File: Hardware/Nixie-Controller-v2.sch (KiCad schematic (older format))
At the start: 219 parts, among them J7 12V DC JACK, J8 RST, U1 MAX1771, U10 74HC4067, U11 M41T01, U12 STM32F103C8, U13 OPA180, U14 74HC4067, U15 OPA180, U16 74HC4067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

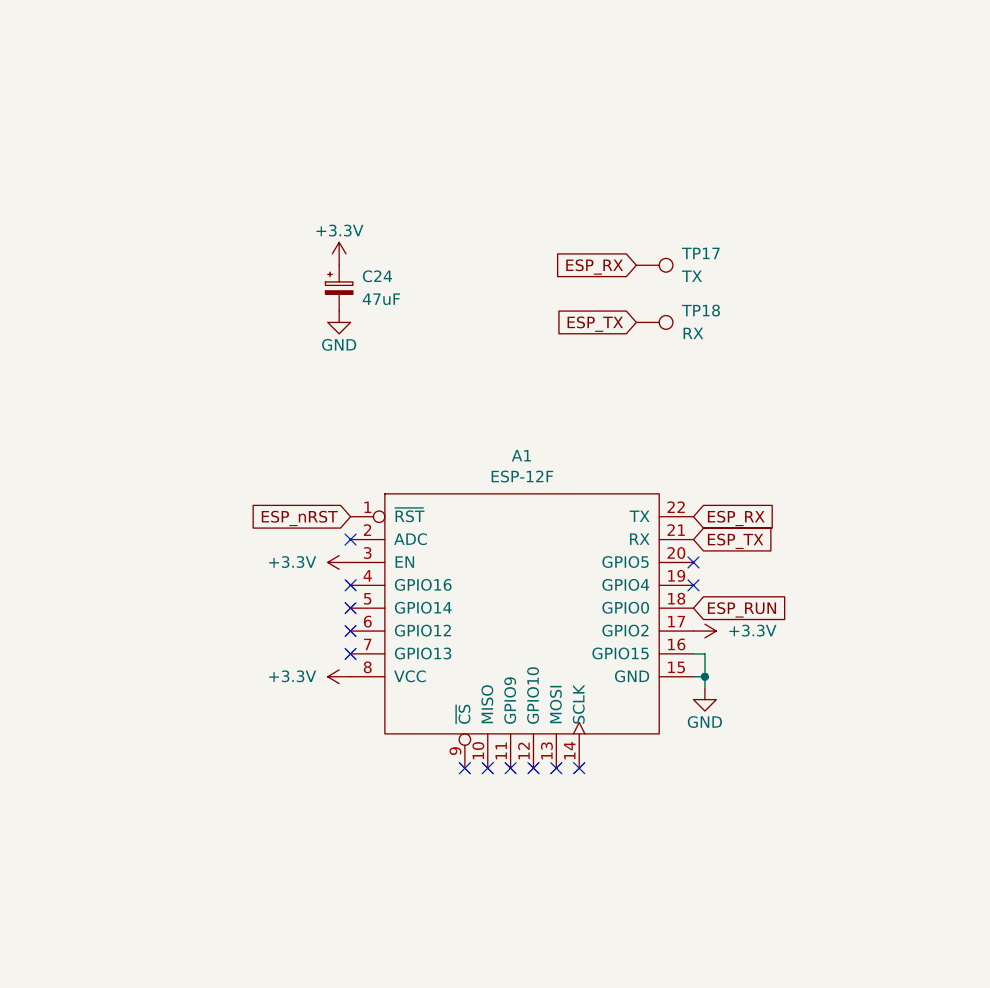
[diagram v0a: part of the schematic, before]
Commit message: Switch to ESP32-WROOM-32E wifi module
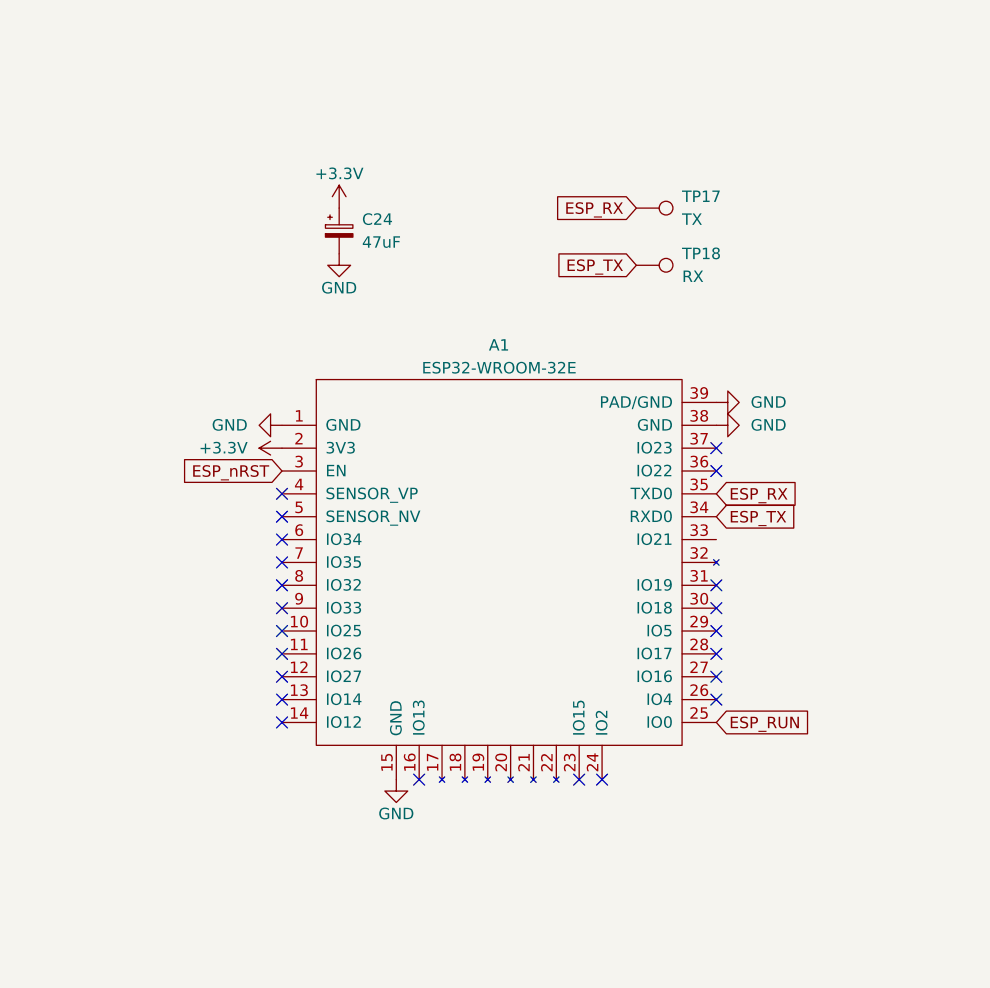
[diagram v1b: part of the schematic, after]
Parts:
- removed A1: ESP-12F, RF_Module:ESP-12E, symbol Nixie-Controller-v2:ESP-12F
- added A1: ESP32-WROOM-32E, RF_Module:ESP32-WROOM-32, symbol Nixie-Controller-v2:ESP32-WROOM-32E
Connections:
- net +3V3: now also A1.2 (3V3)
- net ESP_RUN: now also A1.25 (IO0)
- net ESP_RX: now also A1.35 (TXD0)
- net ESP_TX: now also A1.34 (RXD0)
- net ESP_nRST: now also A1.3 (EN)
- net GND: now also A1.1 (GND), A1.15 (GND), A1.38 (GND), A1.39 (PAD/GND)
- no-connect marks 77 -> 86
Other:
- moved on the sheet: C24, TP17, TP18
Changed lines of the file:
@@
 NoConn ~ 18050 8200
 NoConn ~ 18050 8300
-$Comp
-L Nixie-Controller-v2:ESP-12F A1
-U 1 1 61812F32
-P 30400 8400
-F 0 "A1" H 30400 9015 50  0000 C CNN
-F 1 "ESP-12F" H 30400 8924 50  0000 C CNN
-F 2 "RF_Module:ESP-12E" H 30400 9000 50  0001 C CNN
-F 3 "~" H 30400 9000 50  0001 C CNN
-F 4 "Adafruit" H 30400 8400 50  0001 C CNN "Manufacturer"
-F 5 "2491" H 30400 8400 50  0001 C CNN "Part#"
-	1    30400 8400
-	1    0    0    -1
-$EndComp
-Text GLabel 29650 8050 0    50   Input ~ 0
+Text GLabel 29350 7850 0    50   Input ~ 0
 ESP_nRST
-Text GLabel 31150 8150 2    50   Input ~ 0
+Text GLabel 31250 8050 2    50   Input ~ 0
 ESP_TX
-Text GLabel 31150 8050 2    50   Input ~ 0
+Text GLabel 31250 7950 2    50   Input ~ 0
 ESP_RX
-$Comp
-L power:+3.3V #PWR0216
-U 1 1 618226D2
-P 29650 8750
-F 0 "#PWR0216" H 29650 8600 50  0001 C CNN
-F 1 "+3.3V" V 29650 8900 50  0000 L CNN
-F 2 "" H 29650 8750 50  0001 C CNN
-F 3 "" H 29650 8750 50  0001 C CNN
-	1    29650 8750
-	0    -1   -1   0
-$EndComp
-$Comp
-L power:+3.3V #PWR0129
-U 1 1 618294E9
-P 29650 8250
-F 0 "#PWR0129" H 29650 8100 50  0001 C CNN
-F 1 "+3.3V" V 29650 8400 50  0000 L CNN
-F 2 "" H 29650 8250 50  0001 C CNN
-F 3 "" H 29650 8250 50  0001 C CNN
-	1    29650 8250
-	0    -1   -1   0
-$EndComp
-Text GLabel 31150 8450 2    50   Input ~ 0
+Text GLabel 31250 8950 2    50   Input ~ 0
 ESP_RUN
-$Comp
-L power:GND #PWR0217
-U 1 1 61889434
-P 31200 8800
-F 0 "#PWR0217" H 31200 8550 50  0001 C CNN
-F 1 "GND" H 31200 8650 50  0000 C CNN
-F 2 "" H 31200 8800 50  0001 C CNN
-F 3 "" H 31200 8800 50  0001 C CNN
-	1    31200 8800
-	1    0    0    -1
-$EndComp
-Wire Wire Line
-	31150 8750 31200 8750
-Wire Wire Line
-	31200 8750 31200 8800
-Wire Wire Line
-	31150 8650 31200 8650
-Wire Wire Line
-	31200 8650 31200 8750
-Connection ~ 31200 8750
-$Comp
-L power:+3.3V #PWR0131
-U 1 1 61949ABC
-P 31150 8550
-F 0 "#PWR0131" H 31150 8400 50  0001 C CNN
-F 1 "+3.3V" V 31150 8700 50  0000 L CNN
-F 2 "" H 31150 8550 50  0001 C CNN
-F 3 "" H 31150 8550 50  0001 C CNN
-	1    31150 8550
-	0    1    1    0
-$EndComp
-NoConn ~ 31150 8250
-NoConn ~ 31150 8350
-NoConn ~ 29650 8150
-NoConn ~ 29650 8350
-NoConn ~ 29650 8450
-NoConn ~ 29650 8550
-NoConn ~ 29650 8650
-NoConn ~ 30150 9150
-NoConn ~ 30250 9150
-NoConn ~ 30350 9150
-NoConn ~ 30450 9150
-NoConn ~ 30550 9150
-NoConn ~ 30650 9150
 $Comp
 L Connector:TestPoint TP17
 U 1 1 61DEE128
+P 30900 6700
+F 0 "TP17" V 30850 6900 50  0000 L CNN
+F 1 "TX" V 30950 6900 50  0000 L CNN
+F 2 "TestPoint:TestPoint_Pad_D2.5mm" H 31100 6700 50  0001 C CNN
+F 3 "~" H 31100 6700 50  0001 C CNN
+F 4 "~" H 30900 6700 50  0001 C CNN "Manufacturer"
+F 5 "~" H 30900 6700 50  0001 C CNN "Part#"
+	1    30900 6700
+	0    1    1    0
+$EndComp
+$Comp
+L Connector:TestPoint TP18
+U 1 1 61E4963F
 P 30900 6950
-F 0 "TP17" V 30850 7150 50  0000 L CNN
-F 1 "TX" V 30950 7150 50  0000 L CNN
+F 0 "TP18" V 30850 7150 50  0000 L CNN
+F 1 "RX" V 30950 7150 50  0000 L CNN
 F 2 "TestPoint:TestPoint_Pad_D2.5mm" H 31100 6950 50  0001 C CNN
 F 3 "~" H 31100 6950 50  0001 C CNN
@@
 $EndComp
 $Comp
-L Connector:TestPoint TP18
-U 1 1 61E4963F
-P 30900 7200
-F 0 "TP18" V 30850 7400 50  0000 L CNN
-F 1 "RX" V 30950 7400 50  0000 L CNN
-F 2 "TestPoint:TestPoint_Pad_D2.5mm" H 31100 7200 50  0001 C CNN
-F 3 "~" H 31100 7200 50  0001 C CNN
-F 4 "~" H 30900 7200 50  0001 C CNN "Manufacturer"
-F 5 "~" H 30900 7200 50  0001 C CNN "Part#"
-	1    30900 7200
-	0    1    1    0
-$EndComp
-$Comp
 L Device:CP_Small C24
 U 1 1 61EA48C6
-P 29600 7050
-F 0 "C24" H 29700 7100 50  0000 L CNN
-F 1 "47uF" H 29700 7000 50  0000 L CNN
-F 2 "Capacitor_SMD:CP_Elec_5x5.3" H 29600 7050 50  0001 C CNN
-F 3 "~" H 29600 7050 50  0001 C CNN
-F 4 "Nichicon" H 29600 7050 50  0001 C CNN "Manufacturer"
-F 5 "UWF0J470MCL1GB" H 29600 7050 50  0001 C CNN "Part#"
-	1    29600 7050
+P 29600 6800
+F 0 "C24" H 29700 6850 50  0000 L CNN
+F 1 "47uF" H 29700 6750 50  0000 L CNN
+F 2 "Capacitor_SMD:CP_Elec_5x5.3" H 29600 6800 50  0001 C CNN
+F 3 "~" H 29600 6800 50  0001 C CNN
+F 4 "Nichicon" H 29600 6800 50  0001 C CNN "Manufacturer"
+F 5 "UWF0J470MCL1GB" H 29600 6800 50  0001 C CNN "Part#"
+	1    29600 6800
 	1    0    0    -1
 $EndComp
@@
 L power:GND #PWR0128
 U 1 1 61EA9391
-P 29600 7150
-F 0 "#PWR0128" H 29600 6900 50  0001 C CNN
-F 1 "GND" H 29600 7000 50  0000 C CNN
-F 2 "" H 29600 7150 50  0001 C CNN
-F 3 "" H 29600 7150 50  0001 C CNN
-	1    29600 7150
+P 29600 6900
+F 0 "#PWR0128" H 29600 6650 50  0001 C CNN
+F 1 "GND" H 29600 6750 50  0000 C CNN
+F 2 "" H 29600 6900 50  0001 C CNN
+F 3 "" H 29600 6900 50  0001 C CNN
+	1    29600 6900
 	1    0    0    -1
 $EndComp
@@
 L power:+3.3V #PWR0125
 U 1 1 61F072D5
-P 29600 6950
-F 0 "#PWR0125" H 29600 6800 50  0001 C CNN
-F 1 "+3.3V" H 29600 7100 50  0000 C CNN
-F 2 "" H 29600 6950 50  0001 C CNN
-F 3 "" H 29600 6950 50  0001 C CNN
-	1    29600 6950
-	1    0    0    -1
-$EndComp
-Text GLabel 30900 7200 0    50   Input ~ 0
+P 29600 6700
+F 0 "#PWR0125" H 29600 6550 50  0001 C CNN
+F 1 "+3.3V" H 29600 6850 50  0000 C CNN
+F 2 "" H 29600 6700 50  0001 C CNN
+F 3 "" H 29600 6700 50  0001 C CNN
+	1    29600 6700
+	1    0    0    -1
+$EndComp
+Text GLabel 30900 6950 0    50   Input ~ 0
 ESP_TX
-Text GLabel 30900 6950 0    50   Input ~ 0
+Text GLabel 30900 6700 0    50   Input ~ 0
 ESP_RX
 Text GLabel 16050 8100 0    50   Input ~ 0
@@
 	1    0    0    -1
 $EndComp
+$Comp
+L Nixie-Controller-v2:ESP32-WROOM-32E A1
+U 1 1 61B96031
+P 30300 8300
+F 0 "A1" H 30300 9300 50  0000 C CNN
+F 1 "ESP32-WROOM-32E" H 30300 9200 50  0000 C CNN
+F 2 "RF_Module:ESP32-WROOM-32" H 30300 9200 50  0001 C CNN
+F 3 "" H 30300 9200 50  0001 C CNN
+	1    30300 8300
+	1    0    0    -1
+$EndComp
+$Comp
+L power:GND #PWR0129
+U 1 1 61C53AEF
+P 29350 7650
+F 0 "#PWR0129" H 29350 7400 50  0001 C CNN
+F 1 "GND" V 29350 7500 50  0000 R CNN
+F 2 "" H 29350 7650 50  0001 C CNN
+F 3 "" H 29350 7650 50  0001 C CNN
+	1    29350 7650
+	0    1    1    0
+$EndComp
+$Comp
+L power:+3.3V #PWR0216
+U 1 1 61C5EE42
+P 29350 7750
+F 0 "#PWR0216" H 29350 7600 50  0001 C CNN
+F 1 "+3.3V" V 29350 7900 50  0000 L CNN
+F 2 "" H 29350 7750 50  0001 C CNN
+F 3 "" H 29350 7750 50  0001 C CNN
+	1    29350 7750
+	0    -1   -1   0
+$EndComp
+$Comp
+L power:GND #PWR0131
+U 1 1 61C64FFC
+P 31250 7650
+F 0 "#PWR0131" H 31250 7400 50  0001 C CNN
+F 1 "GND" V 31250 7500 50  0000 R CNN
+F 2 "" H 31250 7650 50  0001 C CNN
+F 3 "" H 31250 7650 50  0001 C CNN
+	1    31250 7650
+	0    -1   -1   0
+$EndComp
+$Comp
+L power:GND #PWR0217
+U 1 1 61C6A12F
+P 29850 9200
+F 0 "#PWR0217" H 29850 8950 50  0001 C CNN
+F 1 "GND" H 29850 9050 50  0000 C CNN
+F 2 "" H 29850 9200 50  0001 C CNN
+F 3 "" H 29850 9200 50  0001 C CNN
+	1    29850 9200
+	1    0    0    -1
+$EndComp
+NoConn ~ 29350 7950
+NoConn ~ 29350 8050
+NoConn ~ 29350 8150
+NoConn ~ 29350 8250
+NoConn ~ 29350 8350
+NoConn ~ 29350 8450
+NoConn ~ 29350 8550
+NoConn ~ 29350 8650
+NoConn ~ 29350 8750
+NoConn ~ 29350 8850
+NoConn ~ 29350 8950
+NoConn ~ 29950 9200
+NoConn ~ 30650 9200
+NoConn ~ 30750 9200
+NoConn ~ 31250 8850
+NoConn ~ 31250 8750
+NoConn ~ 31250 8650
+NoConn ~ 31250 8550
+NoConn ~ 31250 8450
+NoConn ~ 31250 8350
+NoConn ~ 31250 7850
+NoConn ~ 31250 7750
+$Comp
+L power:GND #PWR0218
+U 1 1 62571169
+P 31250 7550
+F 0 "#PWR0218" H 31250 7300 50  0001 C CNN
+F 1 "GND" V 31250 7400 50  0000 R CNN
+F 2 "" H 31250 7550 50  0001 C CNN
+F 3 "" H 31250 7550 50  0001 C CNN
+	1    31250 7550
+	0    -1   -1   0
+$EndComp
 $EndSCHEMATC

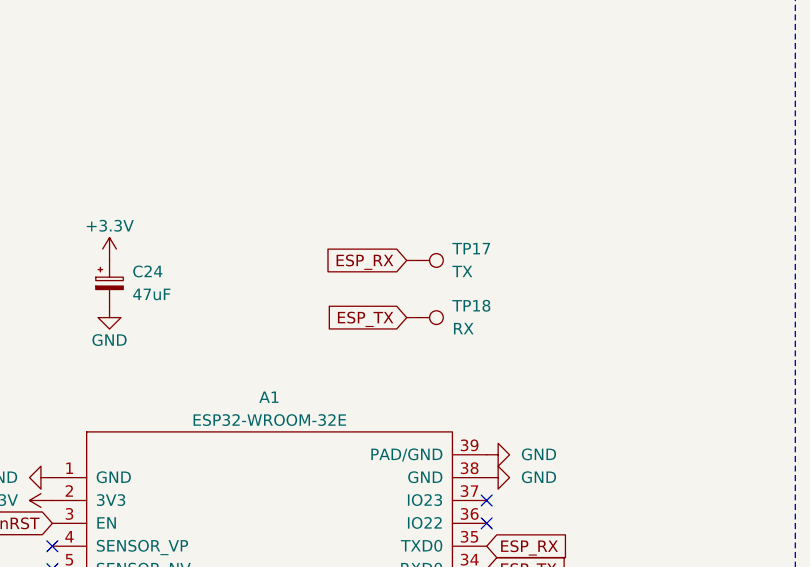
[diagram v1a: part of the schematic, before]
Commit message: Update testpoints & decrease size
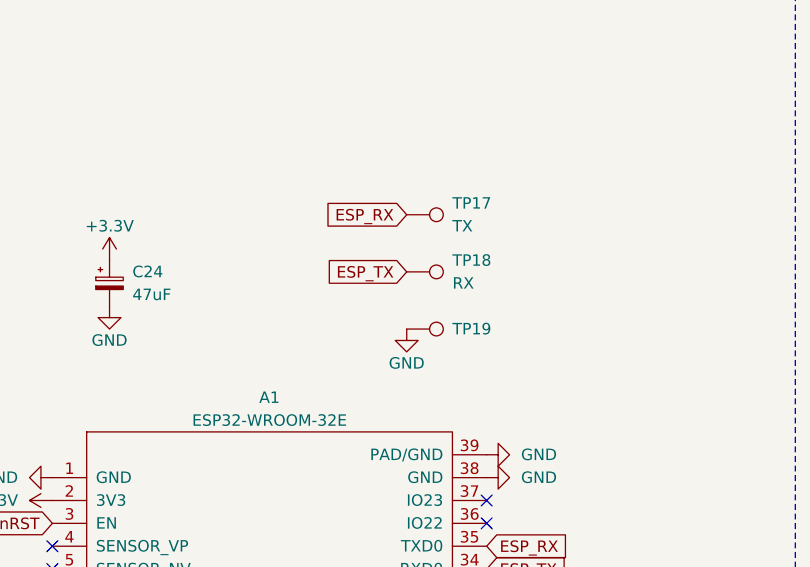
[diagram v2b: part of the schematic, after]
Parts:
- added TP19: ~, TestPoint:TestPoint_Pad_D1.5mm, symbol Connector:TestPoint
- TP1, TP11, TP14, TP15, TP16, TP17, TP18, TP2, TP7: footprint TestPoint:TestPoint_Pad_D2.5mm -> TestPoint:TestPoint_Pad_D1.5mm
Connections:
- net GND: now also TP19.1
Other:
- moved on the sheet: TP17, TP18
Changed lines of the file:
@@
 F 0 "TP2" V 31050 2550 50  0000 L CNN
 F 1 "3.3V" V 31150 2550 50  0000 L CNN
-F 2 "TestPoint:TestPoint_Pad_D2.5mm" H 31300 2350 50  0001 C CNN
+F 2 "TestPoint:TestPoint_Pad_D1.5mm" H 31300 2350 50  0001 C CNN
 F 3 "~" H 31300 2350 50  0001 C CNN
 F 4 "~" H 31100 2350 50  0001 C CNN "Manufacturer"
@@
 F 0 "TP7" V 31050 2800 50  0000 L CNN
 F 1 "5V" V 31150 2800 50  0000 L CNN
-F 2 "TestPoint:TestPoint_Pad_D2.5mm" H 31300 2600 50  0001 C CNN
+F 2 "TestPoint:TestPoint_Pad_D1.5mm" H 31300 2600 50  0001 C CNN
 F 3 "~" H 31300 2600 50  0001 C CNN
 F 4 "~" H 31100 2600 50  0001 C CNN "Manufacturer"
@@
 F 0 "TP11" V 31050 3050 50  0000 L CNN
 F 1 "12V" V 31150 3050 50  0000 L CNN
-F 2 "TestPoint:TestPoint_Pad_D2.5mm" H 31300 2850 50  0001 C CNN
+F 2 "TestPoint:TestPoint_Pad_D1.5mm" H 31300 2850 50  0001 C CNN
 F 3 "~" H 31300 2850 50  0001 C CNN
 F 4 "~" H 31100 2850 50  0001 C CNN "Manufacturer"
@@
 F 0 "TP14" V 31050 3300 50  0000 L CNN
 F 1 "180V" V 31150 3300 50  0000 L CNN
-F 2 "TestPoint:TestPoint_Pad_D2.5mm" H 31300 3100 50  0001 C CNN
+F 2 "TestPoint:TestPoint_Pad_D1.5mm" H 31300 3100 50  0001 C CNN
 F 3 "~" H 31300 3100 50  0001 C CNN
 F 4 "~" H 31100 3100 50  0001 C CNN "Manufacturer"
@@
 F 0 "TP15" V 31050 3550 50  0000 L CNN
 F 1 "GND" V 31150 3550 50  0000 L CNN
-F 2 "TestPoint:TestPoint_Pad_D2.5mm" H 31300 3350 50  0001 C CNN
+F 2 "TestPoint:TestPoint_Pad_D1.5mm" H 31300 3350 50  0001 C CNN
 F 3 "~" H 31300 3350 50  0001 C CNN
 F 4 "~" H 31100 3350 50  0001 C CNN "Manufacturer"
@@
 F 0 "TP1" V 31050 2300 50  0000 L CNN
 F 1 "BATT" V 31150 2300 50  0000 L CNN
-F 2 "TestPoint:TestPoint_Pad_D2.5mm" H 31300 2100 50  0001 C CNN
+F 2 "TestPoint:TestPoint_Pad_D1.5mm" H 31300 2100 50  0001 C CNN
 F 3 "~" H 31300 2100 50  0001 C CNN
 F 4 "~" H 31100 2100 50  0001 C CNN "Manufacturer"
@@
 F 0 "TP16" V 26350 8600 50  0000 L CNN
 F 1 "RTC_CAL" V 26450 8600 50  0000 L CNN
-F 2 "TestPoint:TestPoint_Pad_D2.5mm" H 26600 8400 50  0001 C CNN
+F 2 "TestPoint:TestPoint_Pad_D1.5mm" H 26600 8400 50  0001 C CNN
 F 3 "~" H 26600 8400 50  0001 C CNN
 F 4 "~" H 26400 8400 50  0001 C CNN "Manufacturer"
@@
 L Connector:TestPoint TP17
 U 1 1 61DEE128
-P 30900 6700
-F 0 "TP17" V 30850 6900 50  0000 L CNN
-F 1 "TX" V 30950 6900 50  0000 L CNN
-F 2 "TestPoint:TestPoint_Pad_D2.5mm" H 31100 6700 50  0001 C CNN
-F 3 "~" H 31100 6700 50  0001 C CNN
-F 4 "~" H 30900 6700 50  0001 C CNN "Manufacturer"
-F 5 "~" H 30900 6700 50  0001 C CNN "Part#"
-	1    30900 6700
+P 30900 6500
+F 0 "TP17" V 30850 6700 50  0000 L CNN
+F 1 "TX" V 30950 6700 50  0000 L CNN
+F 2 "TestPoint:TestPoint_Pad_D1.5mm" H 31100 6500 50  0001 C CNN
+F 3 "~" H 31100 6500 50  0001 C CNN
+F 4 "~" H 30900 6500 50  0001 C CNN "Manufacturer"
+F 5 "~" H 30900 6500 50  0001 C CNN "Part#"
+	1    30900 6500
 	0    1    1    0
 $EndComp
@@
 L Connector:TestPoint TP18
 U 1 1 61E4963F
-P 30900 6950
-F 0 "TP18" V 30850 7150 50  0000 L CNN
-F 1 "RX" V 30950 7150 50  0000 L CNN
-F 2 "TestPoint:TestPoint_Pad_D2.5mm" H 31100 6950 50  0001 C CNN
-F 3 "~" H 31100 6950 50  0001 C CNN
-F 4 "~" H 30900 6950 50  0001 C CNN "Manufacturer"
-F 5 "~" H 30900 6950 50  0001 C CNN "Part#"
-	1    30900 6950
+P 30900 6750
+F 0 "TP18" V 30850 6950 50  0000 L CNN
+F 1 "RX" V 30950 6950 50  0000 L CNN
+F 2 "TestPoint:TestPoint_Pad_D1.5mm" H 31100 6750 50  0001 C CNN
+F 3 "~" H 31100 6750 50  0001 C CNN
+F 4 "~" H 30900 6750 50  0001 C CNN "Manufacturer"
+F 5 "~" H 30900 6750 50  0001 C CNN "Part#"
+	1    30900 6750
 	0    1    1    0
 $EndComp
@@
 	1    0    0    -1
 $EndComp
-Text GLabel 30900 6950 0    50   Input ~ 0
+Text GLabel 30900 6750 0    50   Input ~ 0
 ESP_TX
-Text GLabel 30900 6700 0    50   Input ~ 0
+Text GLabel 30900 6500 0    50   Input ~ 0
 ESP_RX
 Text GLabel 16050 8100 0    50   Input ~ 0
@@
 	0    -1   -1   0
 $EndComp
+$Comp
+L Connector:TestPoint TP19
+U 1 1 61961BB9
+P 30900 7000
+F 0 "TP19" V 30900 7200 50  0000 L CNN
+F 1 "~" H 30958 7027 50  0000 L CNN
+F 2 "TestPoint:TestPoint_Pad_D1.5mm" H 31100 7000 50  0001 C CNN
+F 3 "~" H 31100 7000 50  0001 C CNN
+F 4 "~" H 30900 7000 50  0001 C CNN "Manufacturer"
+F 5 "~" H 30900 7000 50  0001 C CNN "Part#"
+	1    30900 7000
+	0    1    1    0
+$EndComp
+$Comp
+L power:GND #PWR0219
+U 1 1 61A1640E
+P 30900 7000
+F 0 "#PWR0219" H 30900 6750 50  0001 C CNN
+F 1 "GND" H 30900 6850 50  0000 C CNN
+F 2 "" H 30900 7000 50  0001 C CNN
+F 3 "" H 30900 7000 50  0001 C CNN
+	1    30900 7000
+	1    0    0    -1
+$EndComp
 $EndSCHEMATC

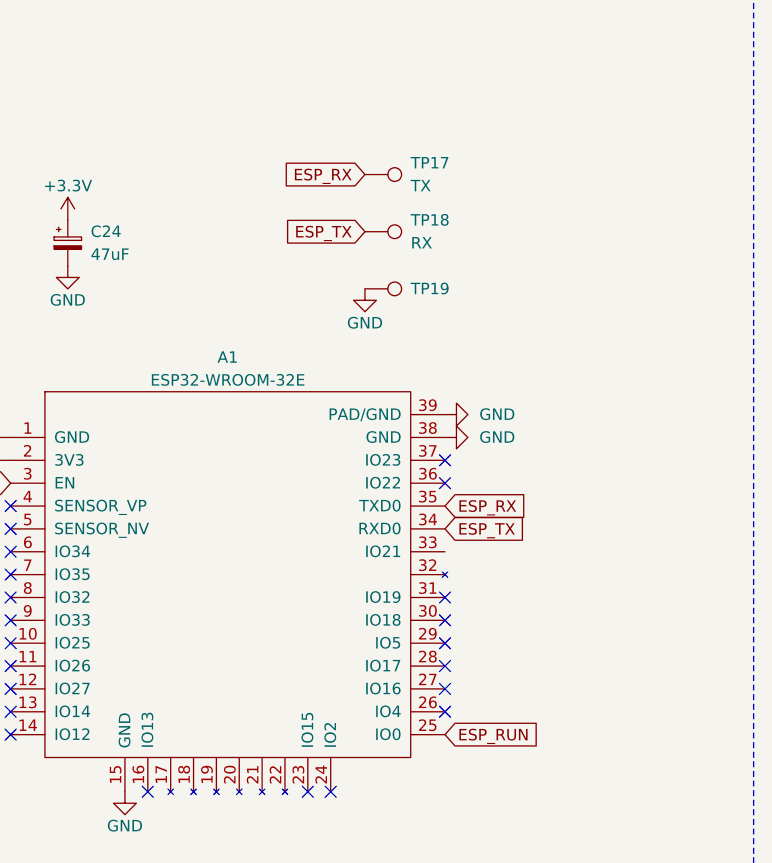
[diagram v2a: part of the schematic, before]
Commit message: Use correct UART ports for ESP32-WROOM-32
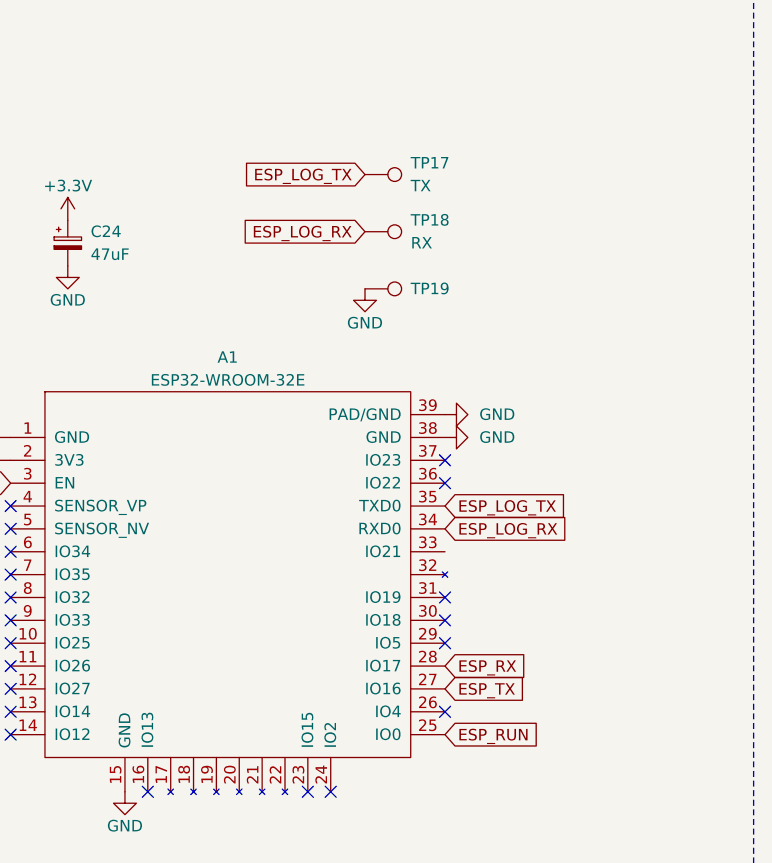
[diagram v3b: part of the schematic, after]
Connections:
- net ESP_RX: now also A1.28 (IO17); no longer A1.35 (TXD0), TP17.1
- net ESP_TX: now also A1.27 (IO16); no longer A1.34 (RXD0), TP18.1
- new net ESP_LOG_RX: A1.34 (RXD0), TP18.1
- new net ESP_LOG_TX: A1.35 (TXD0), TP17.1
- no-connect marks 86 -> 84
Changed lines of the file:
@@
 Text GLabel 29350 7850 0    50   Input ~ 0
 ESP_nRST
-Text GLabel 31250 8050 2    50   Input ~ 0
+Text GLabel 31250 8750 2    50   Input ~ 0
 ESP_TX
-Text GLabel 31250 7950 2    50   Input ~ 0
+Text GLabel 31250 8650 2    50   Input ~ 0
 ESP_RX
 Text GLabel 31250 8950 2    50   Input ~ 0
@@
 	1    0    0    -1
 $EndComp
-Text GLabel 30900 6750 0    50   Input ~ 0
-ESP_TX
-Text GLabel 30900 6500 0    50   Input ~ 0
-ESP_RX
 Text GLabel 16050 8100 0    50   Input ~ 0
 ESP_nRST
@@
 NoConn ~ 30750 9200
 NoConn ~ 31250 8850
-NoConn ~ 31250 8750
-NoConn ~ 31250 8650
 NoConn ~ 31250 8550
 NoConn ~ 31250 8450
@@
 	1    0    0    -1
 $EndComp
+Text GLabel 30900 6750 0    50   Input ~ 0
+ESP_LOG_RX
+Text GLabel 30900 6500 0    50   Input ~ 0
+ESP_LOG_TX
+Text GLabel 31250 8050 2    50   Input ~ 0
+ESP_LOG_RX
+Text GLabel 31250 7950 2    50   Input ~ 0
+ESP_LOG_TX
 $EndSCHEMATC
